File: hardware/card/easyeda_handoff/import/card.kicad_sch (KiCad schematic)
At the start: 2 parts, among them U5 DRV2605LDGS

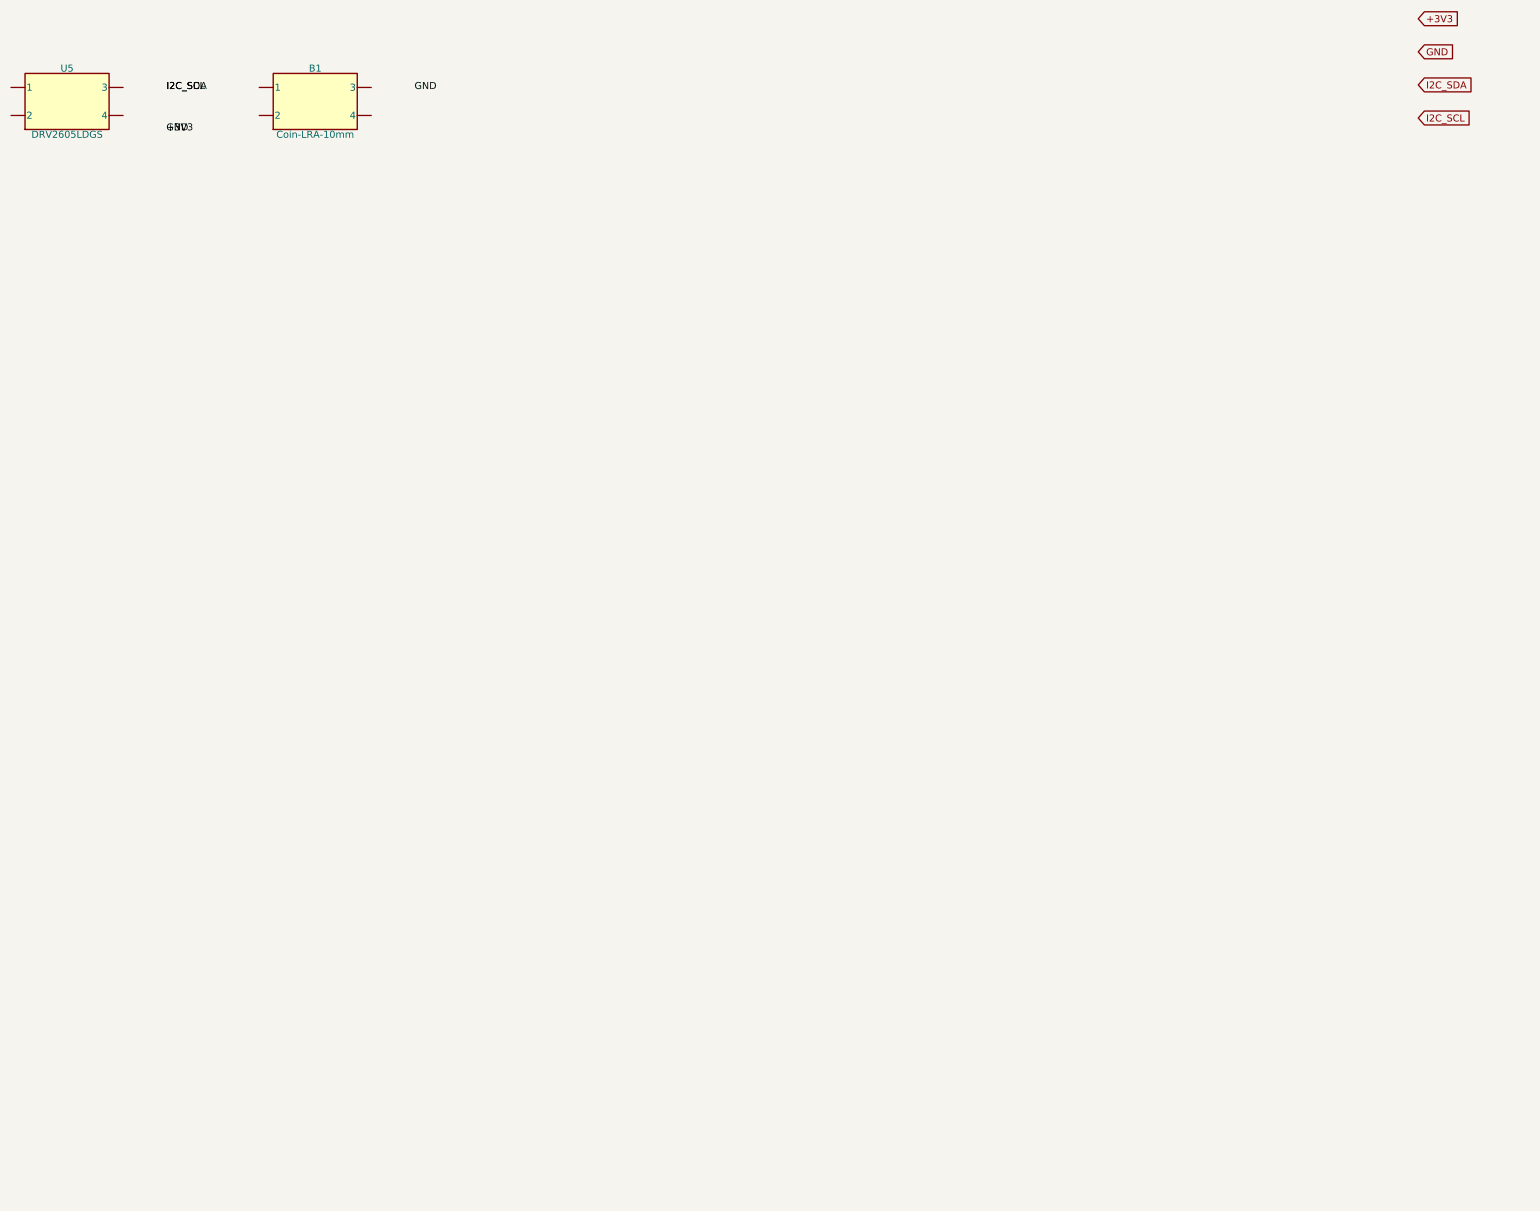
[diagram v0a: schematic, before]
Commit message: Add handheld card EasyEDA handoff
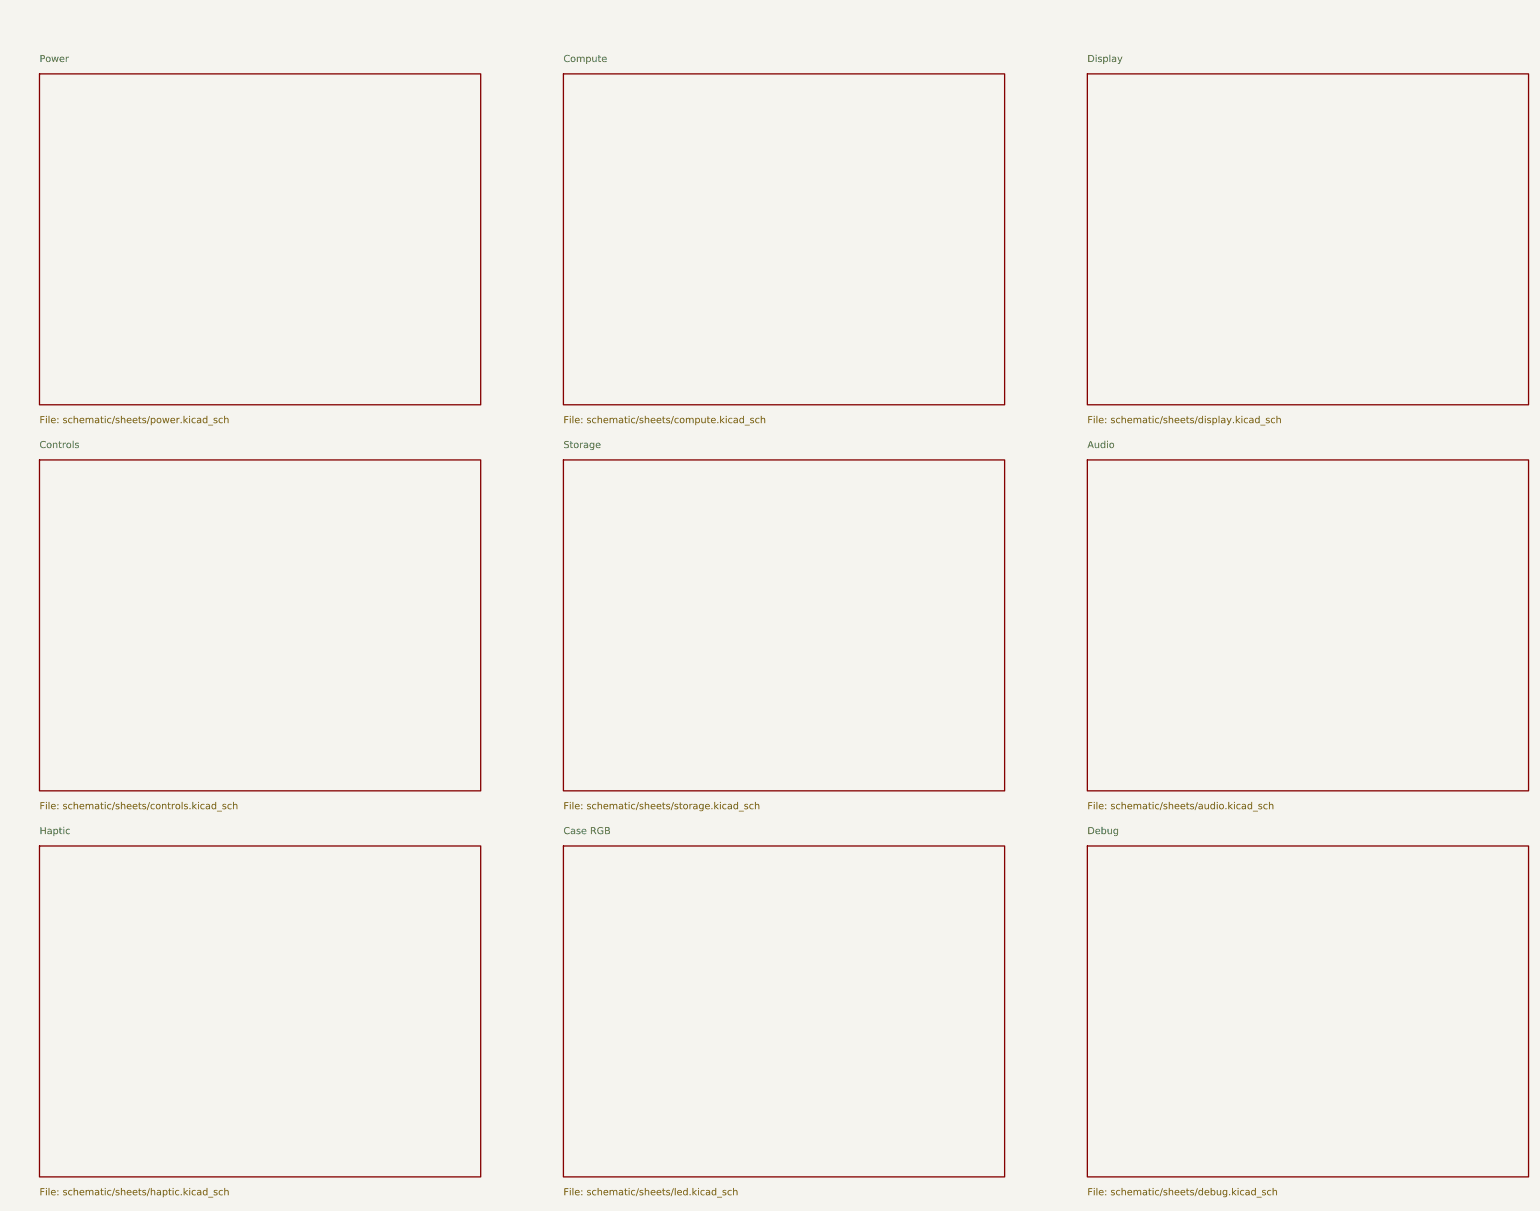
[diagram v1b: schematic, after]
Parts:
- removed B1: Coin-LRA-10mm, TBD, symbol PSCard:Block2
- removed U5: DRV2605LDGS, VSSOP-10-DGS-3x4.9, symbol PSCard:Block2
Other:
- added sheet Audio (schematic/sheets/audio.kicad_sch)
- added sheet Case RGB (schematic/sheets/led.kicad_sch)
- added sheet Compute (schematic/sheets/compute.kicad_sch)
- added sheet Controls (schematic/sheets/controls.kicad_sch)
- added sheet Debug (schematic/sheets/debug.kicad_sch)
- added sheet Display (schematic/sheets/display.kicad_sch)
- added sheet Haptic (schematic/sheets/haptic.kicad_sch)
- added sheet Power (schematic/sheets/power.kicad_sch)
- added sheet Storage (schematic/sheets/storage.kicad_sch)
- title: PuzzleScript Card — haptic -> PuzzleScript Card
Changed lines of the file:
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@@
   (generator "PuzzleScript generate_kicad.js")
   (generator_version "1.0")
-  (paper "A4")
+  (paper "A3")
   (title_block
-    (title "PuzzleScript Card — haptic")
+    (title "PuzzleScript Card")
     (date "2026-07-09")
     (rev "spin1")
-    (comment 1 "Auto-generated from connectivity.json")
-    (comment 2 "Same-net labels connect; globals cross sheets")
   )
-  (symbol (lib_id "PSCard:Block2") (at 35 35 0) (unit 1)
-    (exclude_from_sim no) (in_bom yes) (on_board yes) (dnp no) (fields_autoplaced)
-    (property "Reference" "U5" (at 35 29 0)
-      (effects (font (size 1.27 1.27))))
-    (property "Value" "DRV2605LDGS" (at 35 41 0)
-      (effects (font (size 1.27 1.27))))
-    (property "Footprint" "VSSOP-10-DGS-3x4.9" (at 35 35 0)
-      (effects (font (size 1.27 1.27)) hide))
-    (property "Datasheet" "~" (at 35 35 0)
-      (effects (font (size 1.27 1.27)) hide))
-    (instances (project "card" (path "/card/sheets/haptic" (reference "U5") (unit 1))))
+  (sheet (at 30 30) (size 80 60) (fields_autoplaced)
+    (stroke (width 0.1524) (type solid)) (fill (type none))
+    (property "Sheetname" "Power" (at 30 28 0)
+      (effects (font (size 1.27 1.27)) (justify left bottom)))
+    (property "Sheetfile" "schematic/sheets/power.kicad_sch" (at 30 92 0)
+      (effects (font (size 1.27 1.27)) (justify left top)))
   )
-  (label "+3V3" (at 53 40 0) (fields_autoplaced)
-    (effects (font (size 1.27 1.27)) (justify left)))
-  (label "GND" (at 53 40 0) (fields_autoplaced)
-    (effects (font (size 1.27 1.27)) (justify left)))
-  (label "I2C_SDA" (at 53 32.5 0) (fields_autoplaced)
-    (effects (font (size 1.27 1.27)) (justify left)))
-  (label "I2C_SCL" (at 53 32.5 0) (fields_autoplaced)
-    (effects (font (size 1.27 1.27)) (justify left)))
-  (symbol (lib_id "PSCard:Block2") (at 80 35 0) (unit 1)
-    (exclude_from_sim no) (in_bom yes) (on_board yes) (dnp no) (fields_autoplaced)
-    (property "Reference" "B1" (at 80 29 0)
-      (effects (font (size 1.27 1.27))))
-    (property "Value" "Coin-LRA-10mm" (at 80 41 0)
-      (effects (font (size 1.27 1.27))))
-    (property "Footprint" "TBD" (at 80 35 0)
-      (effects (font (size 1.27 1.27)) hide))
-    (property "Datasheet" "~" (at 80 35 0)
-      (effects (font (size 1.27 1.27)) hide))
-    (property "Gate" "GATE-LRA-MOUNT" (at 80 35 0)
-      (effects (font (size 1.27 1.27)) hide))
-    (instances (project "card" (path "/card/sheets/haptic" (reference "B1") (unit 1))))
+  (sheet (at 125 30) (size 80 60) (fields_autoplaced)
+    (stroke (width 0.1524) (type solid)) (fill (type none))
+    (property "Sheetname" "Compute" (at 125 28 0)
+      (effects (font (size 1.27 1.27)) (justify left bottom)))
+    (property "Sheetfile" "schematic/sheets/compute.kicad_sch" (at 125 92 0)
+      (effects (font (size 1.27 1.27)) (justify left top)))
   )
-  (label "GND" (at 98 32.5 0) (fields_autoplaced)
-    (effects (font (size 1.27 1.27)) (justify left)))
-  (global_label "+3V3" (shape input) (at 280 20 0) (fields_autoplaced)
-    (effects (font (size 1.27 1.27)) (justify left))
-    (property "Intersheetrefs" "${INTERSHEET_REFS}" (at 280 20 0)
-      (effects (font (size 1.27 1.27)) hide))
+  (sheet (at 220 30) (size 80 60) (fields_autoplaced)
+    (stroke (width 0.1524) (type solid)) (fill (type none))
+    (property "Sheetname" "Display" (at 220 28 0)
+      (effects (font (size 1.27 1.27)) (justify left bottom)))
+    (property "Sheetfile" "schematic/sheets/display.kicad_sch" (at 220 92 0)
+      (effects (font (size 1.27 1.27)) (justify left top)))
   )
-  (global_label "GND" (shape input) (at 280 26 0) (fields_autoplaced)
-    (effects (font (size 1.27 1.27)) (justify left))
-    (property "Intersheetrefs" "${INTERSHEET_REFS}" (at 280 26 0)
-      (effects (font (size 1.27 1.27)) hide))
+  (sheet (at 30 100) (size 80 60) (fields_autoplaced)
+    (stroke (width 0.1524) (type solid)) (fill (type none))
+    (property "Sheetname" "Controls" (at 30 98 0)
+      (effects (font (size 1.27 1.27)) (justify left bottom)))
+    (property "Sheetfile" "schematic/sheets/controls.kicad_sch" (at 30 162 0)
+      (effects (font (size 1.27 1.27)) (justify left top)))
   )
-  (global_label "I2C_SDA" (shape input) (at 280 32 0) (fields_autoplaced)
-    (effects (font (size 1.27 1.27)) (justify left))
-    (property "Intersheetrefs" "${INTERSHEET_REFS}" (at 280 32 0)
-      (effects (font (size 1.27 1.27)) hide))
+  (sheet (at 125 100) (size 80 60) (fields_autoplaced)
+    (stroke (width 0.1524) (type solid)) (fill (type none))
+    (property "Sheetname" "Storage" (at 125 98 0)
+      (effects (font (size 1.27 1.27)) (justify left bottom)))
+    (property "Sheetfile" "schematic/sheets/storage.kicad_sch" (at 125 162 0)
+      (effects (font (size 1.27 1.27)) (justify left top)))
   )
-  (global_label "I2C_SCL" (shape input) (at 280 38 0) (fields_autoplaced)
-    (effects (font (size 1.27 1.27)) (justify left))
-    (property "Intersheetrefs" "${INTERSHEET_REFS}" (at 280 38 0)
-      (effects (font (size 1.27 1.27)) hide))
+  (sheet (at 220 100) (size 80 60) (fields_autoplaced)
+    (stroke (width 0.1524) (type solid)) (fill (type none))
+    (property "Sheetname" "Audio" (at 220 98 0)
+      (effects (font (size 1.27 1.27)) (justify left bottom)))
+    (property "Sheetfile" "schematic/sheets/audio.kicad_sch" (at 220 162 0)
+      (effects (font (size 1.27 1.27)) (justify left top)))
+  )
+  (sheet (at 30 170) (size 80 60) (fields_autoplaced)
+    (stroke (width 0.1524) (type solid)) (fill (type none))
+    (property "Sheetname" "Haptic" (at 30 168 0)
+      (effects (font (size 1.27 1.27)) (justify left bottom)))
+    (property "Sheetfile" "schematic/sheets/haptic.kicad_sch" (at 30 232 0)
+      (effects (font (size 1.27 1.27)) (justify left top)))
+  )
+  (sheet (at 125 170) (size 80 60) (fields_autoplaced)
+    (stroke (width 0.1524) (type solid)) (fill (type none))
+    (property "Sheetname" "Case RGB" (at 125 168 0)
+      (effects (font (size 1.27 1.27)) (justify left bottom)))
+    (property "Sheetfile" "schematic/sheets/led.kicad_sch" (at 125 232 0)
+      (effects (font (size 1.27 1.27)) (justify left top)))
+  )
+  (sheet (at 220 170) (size 80 60) (fields_autoplaced)
+    (stroke (width 0.1524) (type solid)) (fill (type none))
+    (property "Sheetname" "Debug" (at 220 168 0)
+      (effects (font (size 1.27 1.27)) (justify left bottom)))
+    (property "Sheetfile" "schematic/sheets/debug.kicad_sch" (at 220 232 0)
+      (effects (font (size 1.27 1.27)) (justify left top)))
   )
 )
